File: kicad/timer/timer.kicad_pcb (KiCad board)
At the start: 4 copper layers, 86.4 x 63.5 mm, 13 parts, among them SW1 SW_Push, U1 ATmega328P-P, Y1 Crystal

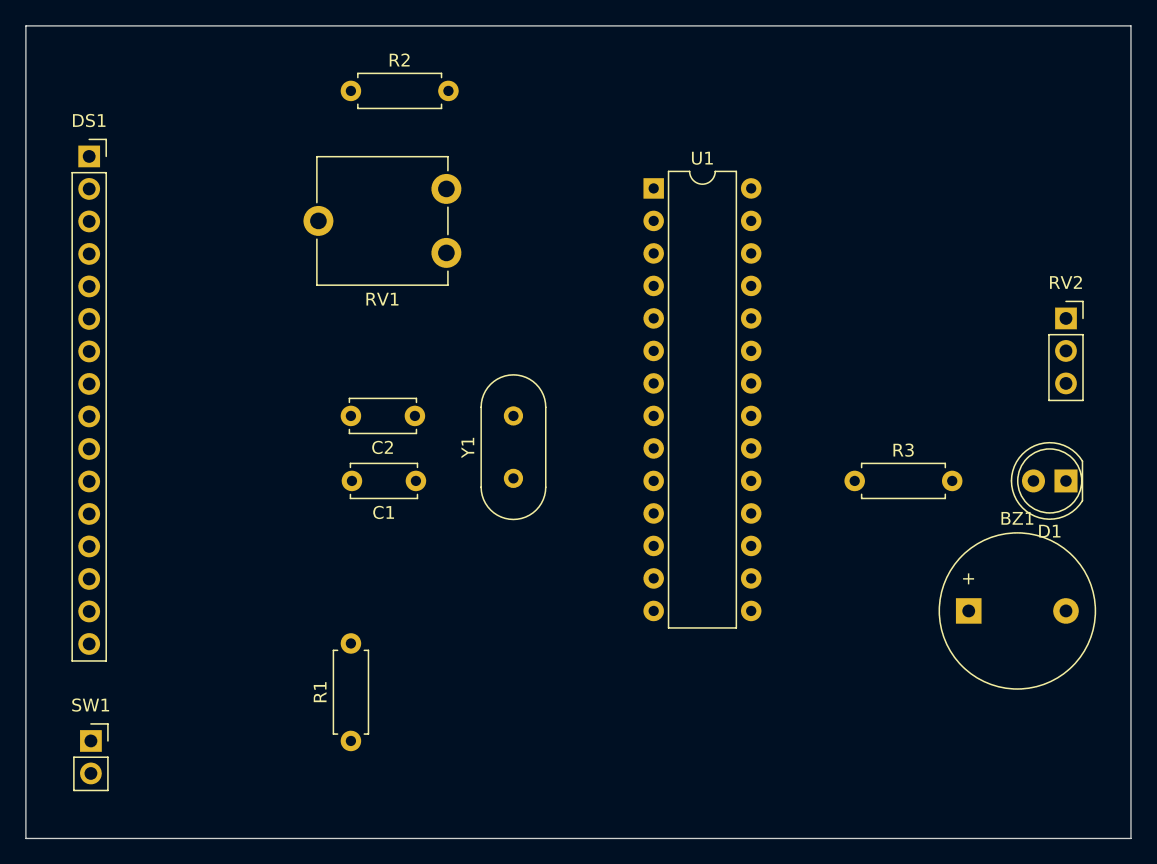
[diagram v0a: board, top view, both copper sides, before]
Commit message: Add voltage regulator
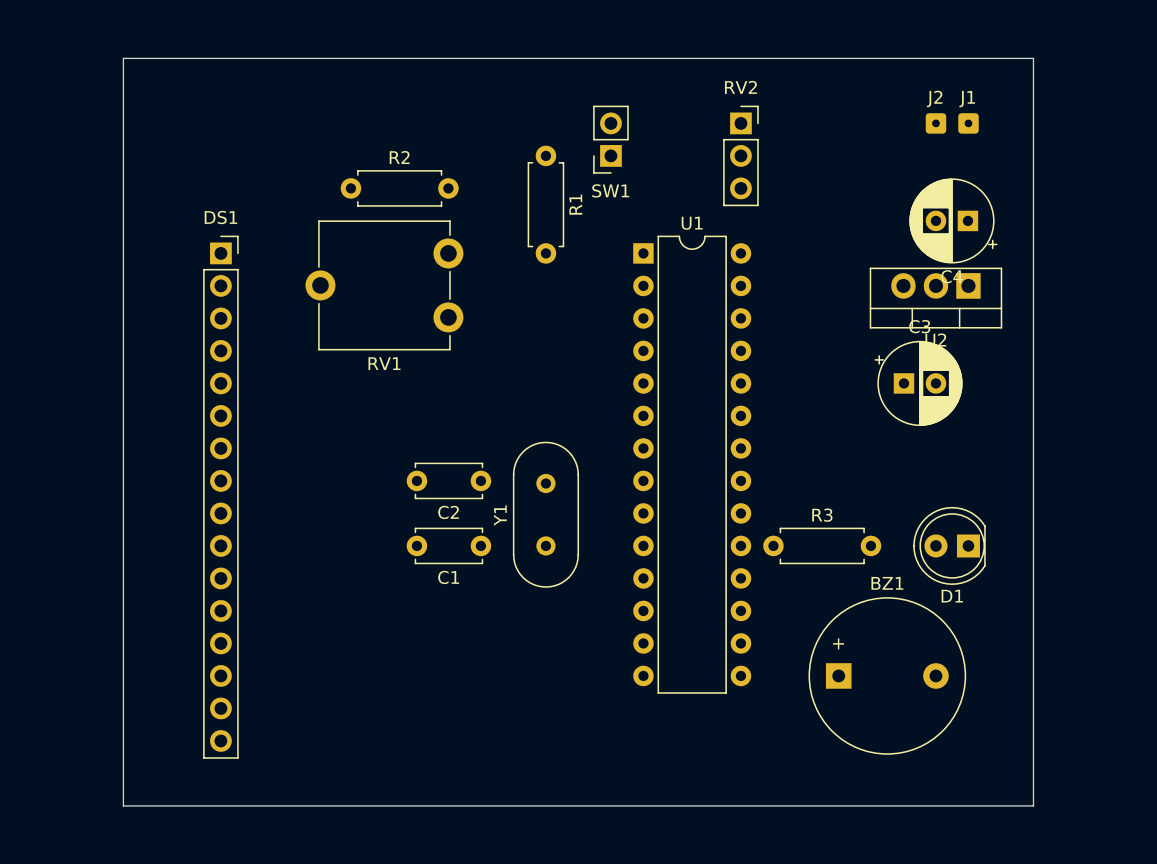
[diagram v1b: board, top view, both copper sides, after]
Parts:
- added C3: 100µ, Capacitor_THT:CP_Radial_D6.3mm_P2.50mm, F.Cu at (152.4, 94.0)
- added C4: 100µ, Capacitor_THT:CP_Radial_D6.3mm_P2.50mm, F.Cu at (157.4, 81.3)
- added J1: Conn_01x01_Pin, Connector_Wire:SolderWire-0.1sqmm_1x01_D0.4mm_OD1mm, F.Cu at (157.5, 73.7)
- added J2: Conn_01x01_Pin, Connector_Wire:SolderWire-0.1sqmm_1x01_D0.4mm_OD1mm, F.Cu at (154.9, 73.7)
- added U2: L7805, Package_TO_SOT_THT:TO-220-3_Vertical, F.Cu at (157.5, 86.4)
- C1, C2: value C -> 22p
- moved SW1 61.2 mm to (129.5, 76.2), turned to 180 degrees
- moved R1 48.2 mm to (124.5, 76.2), turned to -90 degrees
- moved RV2 29.6 mm to (139.7, 73.7)
- moved DS1 12.8 mm to (99.1, 83.8)
- moved BZ1 11.4 mm to (147.3, 116.8)
- moved D1 9.16 mm to (157.5, 106.7)
- moved R3 8.13 mm to (142.2, 106.7)
- moved R2 7.62 mm to (109.2, 78.7)
- moved C2 7.24 mm to (119.4, 101.6)
- moved C1 7.18 mm to (119.4, 106.7)
- moved Y1 5.86 mm to (124.5, 106.7)
- moved U1 5.14 mm to (132.1, 83.8)
- moved RV1 5.04 mm to (116.8, 83.8)
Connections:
- R1 pad 1: Net-(U1-PB0) -> Net-(U1-PD2)
- SW1 pad 1: Net-(U1-PB0) -> Net-(U1-PD2)
- U1 pad 11: Net-(DS1-D5) -> Net-(DS1-D4)
- U1 pad 12: Net-(DS1-D6) -> Net-(DS1-D5)
- U1 pad 13: Net-(DS1-D7) -> Net-(DS1-D6)
- U1 pad 14: Net-(U1-PB0) -> Net-(DS1-D7)
- U1 pad 4: Net-(DS1-RS) -> Net-(U1-PD2)
- U1 pad 5: Net-(DS1-E) -> Net-(DS1-RS)
- U1 pad 6: Net-(DS1-D4) -> Net-(DS1-E)
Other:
- board size 86.4 x 63.5 mm -> 71.1 x 58.4 mm

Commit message: Route wire tracks
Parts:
- moved DS1 7.62 mm to (106.7, 83.8)
- moved R2 5.08 mm to (114.3, 78.7)
- moved RV1 5.08 mm to (121.9, 83.8)
- moved SW1 2.54 mm to (132.1, 76.2)
- moved R1 2.54 mm to (127.0, 76.2)
- moved BZ1 2.54 mm to (144.8, 116.8)
- moved C3 2.54 mm to (149.9, 94.0)
- moved C4 2.54 mm to (154.9, 81.3)
- moved J1 2.54 mm to (154.9, 73.7)
- moved J2 2.54 mm to (152.4, 73.7)
- moved U2 2.54 mm to (154.9, 86.4)
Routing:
- net GND: track 0.00 -> 258.3 mm
- net +5V: track 0.00 -> 82.2 mm
- net Net-(DS1-RS): track 0.00 -> 26.5 mm
- net Net-(DS1-E): track 0.00 -> 25.4 mm
- net Net-(DS1-D7): track 0.00 -> 25.4 mm
- net Net-(DS1-D6): track 0.00 -> 25.4 mm
- net Net-(DS1-D5): track 0.00 -> 25.4 mm
- net Net-(DS1-D4): track 0.00 -> 25.4 mm
- net Net-(U1-PC0): track 0.00 -> 22.4 mm
- net Net-(U1-PD2): track 0.00 -> 20.9 mm
- net Net-(U1-XTAL1/PB6): track 0.00 -> 13.9 mm
- net +9V: track 0.00 -> 12.7 mm
- net Net-(U1-XTAL2/PB7): track 0.00 -> 12.7 mm
- net Net-(DS1-VDD): track 0.00 -> 10.8 mm
- net Net-(BZ1-+): track 0.00 -> 7.64 mm
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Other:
- board size 71.1 x 58.4 mm -> 58.4 x 53.3 mm

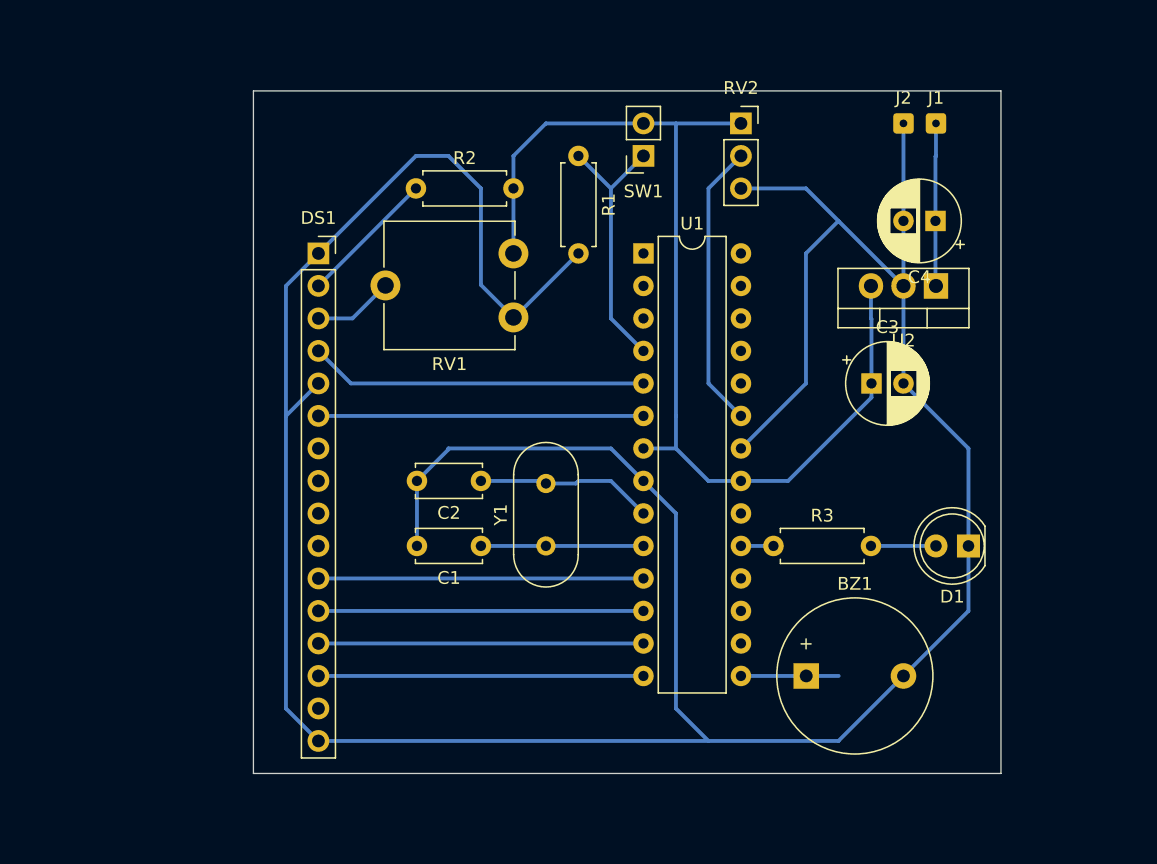
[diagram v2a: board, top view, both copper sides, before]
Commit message: Add missing connection of LCD/LED+ to +5V
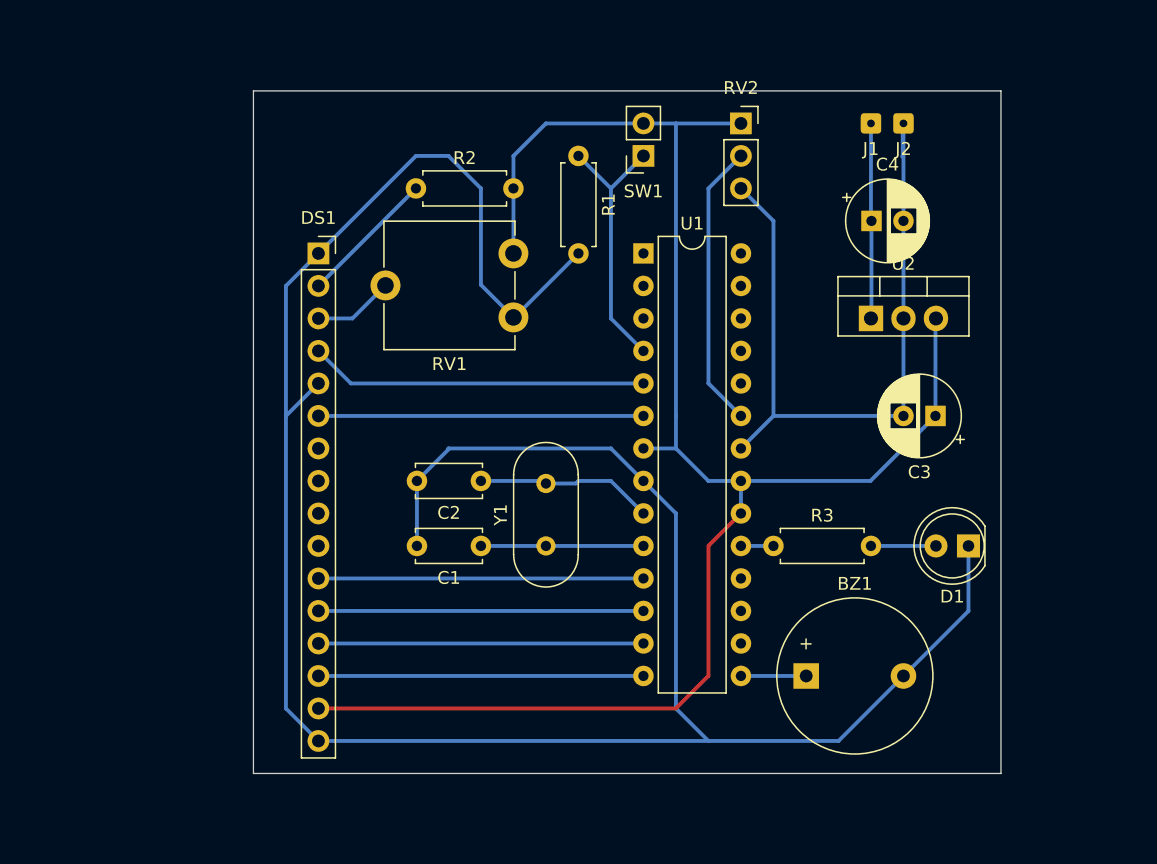
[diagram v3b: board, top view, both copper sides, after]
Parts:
- moved U2 5.68 mm to (149.9, 88.9), turned to 0 degrees
- moved C3 5.61 mm to (154.9, 96.5), turned to 180 degrees
- moved J1 5.08 mm to (149.9, 73.7), turned to 180 degrees
- moved C4 5.00 mm to (149.9, 81.3), turned to 0 degrees
- turned J2 to 180 degrees
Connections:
- DS1 pad 15: unconnected-(DS1-LED(+)-Pad15) -> +5V
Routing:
- net +5V: track 82.2 -> 133.3 mm
- net GND: track 258.3 -> 244.5 mm
- net +9V: track 12.7 -> 15.3 mm
- net Net-(BZ1-+): track 7.64 -> 5.10 mm
